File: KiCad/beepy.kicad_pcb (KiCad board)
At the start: 4 copper layers, 74 x 104 mm, 160 parts, among them J1 FDX0019B1, J10 FDX0019B1, J11 FDX0019B1, J12 FDX0019B1, J13 FDX0019B1, J14 FDX0019B1, J15 USB_C_Receptacle_USB2.0, J16 FDX0019B1, J17 FDX0019B1, J18 FDX0019B1, J19 FDX0019B1, J2 FDX0019B1, J20 FDX0019B1, J21 FDX0019B1, J23 FDX0019B1, J24 FDX0019B1, J25 FDX0019B1, J26 FDX0019B1, J27 FDX0019B1, J28 FDX0019B1, J29 FDX0019B1, J3 FDX0019B1, J30 FDX0019B1, J31 FDX0019B1, J32 FDX0019B1, J33 FDX0019B1, J34 FDX0019B1, J35 FDX0019B1, J36 FDX0019B1, J37 FDX0019B1, J38 FDX0019B1, J39 FDX0019B1, J4 FDX0019B1, J40 FDX0019B1, J41 FDX0019B1, J42 FDX0019B1, J43 Battery, J44 Header 1, J45 PRG_HEADER, J46 Header 2, J47 Header 3, J5 FDX0019B1, J6 FDX0019B1, J7 FDX0019B1, J8 FDX0019B1, J9 FDX0019B1, M1 MountingHole_2.5mm_Pad, M2 MountingHole_2.5mm_Pad, M3 MountingHole_2.5mm_Pad, M4 MountingHole_2.5mm_Pad, Q1 SI2301, Q2 SI2301, Q3 BSS138, Q4 BSS138, Q5 BSS138, Q6 BSS138, Q7 BSS138, Q8 BSS138, Q9 S8050, SW1 ON/OFF, SW2 Button, U1 TP4054, U2 TPS61090, U3 LS027B7DH01, U4 AP2112K-3.3, U5 GD25Q16xS, U6 RP2040, U7 ME6212C18M5G, U8 ME6212C28M5G, U9 BBQ20KBD, Y1 XYDBPCNANF-12MHZ

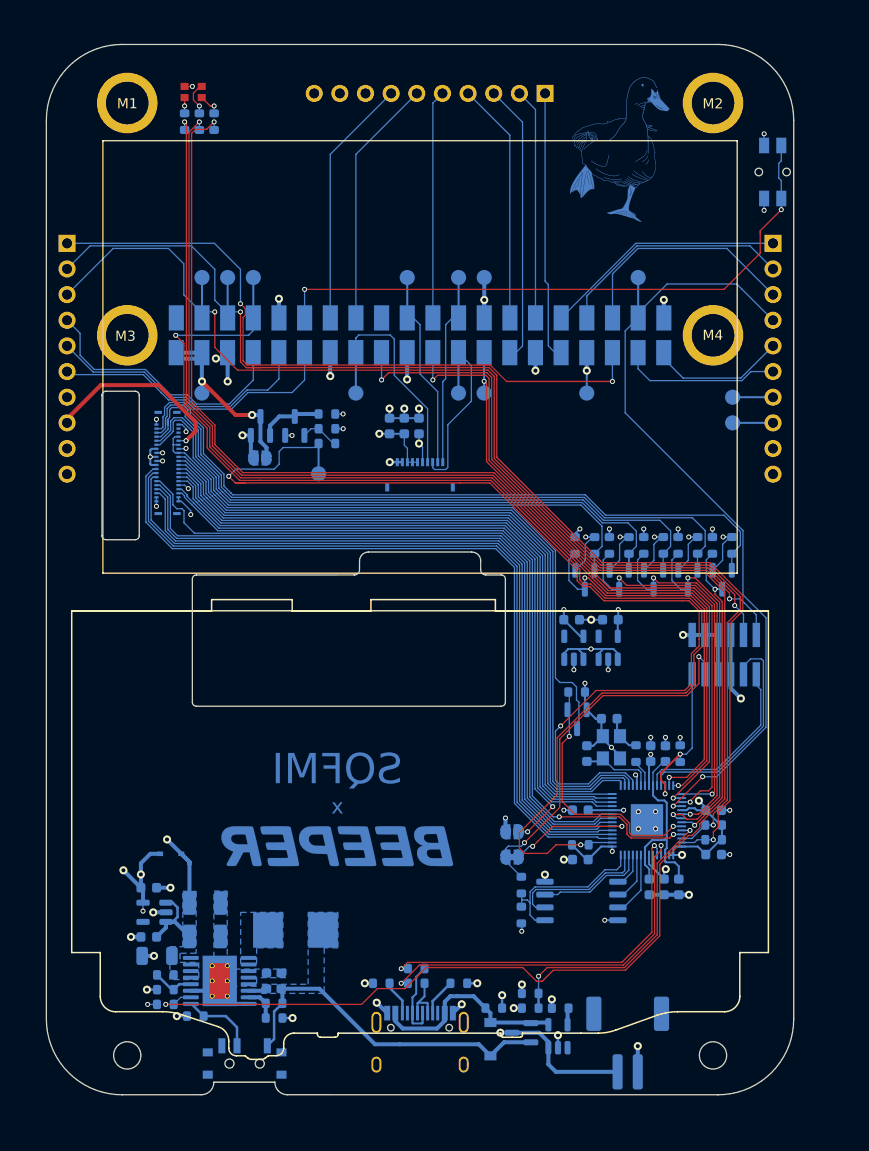
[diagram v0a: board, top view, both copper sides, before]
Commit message: Moved 4 layers to 2 layers with ground fill
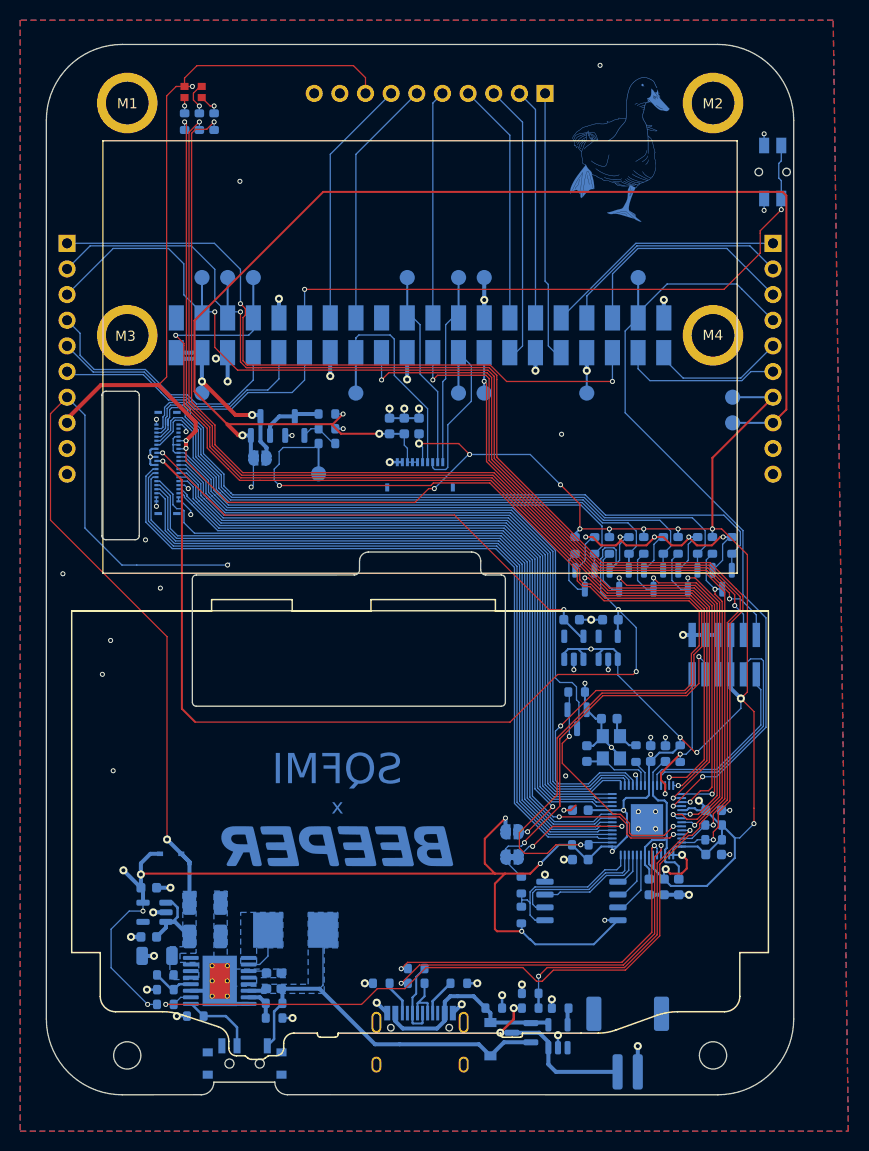
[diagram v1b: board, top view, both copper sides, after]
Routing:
- net +5V: track 164.4 -> 230.3 mm, vias 4 -> 6
- net +3V3: track 449.0 -> 399.8 mm, vias 25 -> 31
- net +1V8: track 100.1 -> 135.0 mm, vias 7 -> 8
- net /Pi_PWR: track 104.6 -> 95.4 mm
- net Net-(C1-Pad1): track 36.2 -> 42.2 mm
- net Net-(L1-Pad2): track 0.00 -> 4.83 mm
- net GND: track 104.3 -> 107.5 mm, vias 58 -> 68
- net +2V8: track 53.9 -> 50.7 mm
- net /keyboard/KB_BL: track 25.3 -> 23.1 mm
- net BOOTSEL: track 38.0 -> 38.8 mm
- added copper zone on F.Cu, net GND
- removed copper zone on In1.Cu, net GND
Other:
- copper layers 4 -> 2
- board text added: "REF**"
- board text removed: "locked"
